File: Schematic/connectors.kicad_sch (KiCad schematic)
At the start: 42 parts, among them U14 HDGC1002WR-S-4P, U15 HDGC1002WR-S-4P, U16 HDGC1002WR-S-4P, U17 HDGC1002WR-S-4P, U18 HDGC1002WR-S-4P, U19 HDGC1002WR-S-4P, U20 HDGC1002WR-S-4P, U21 HDGC1002WR-S-8P, U22 HDGC1002WR-S-8P, U23 HDGC1002WR-S-6P, U24 HDGC1002WR-S-6P

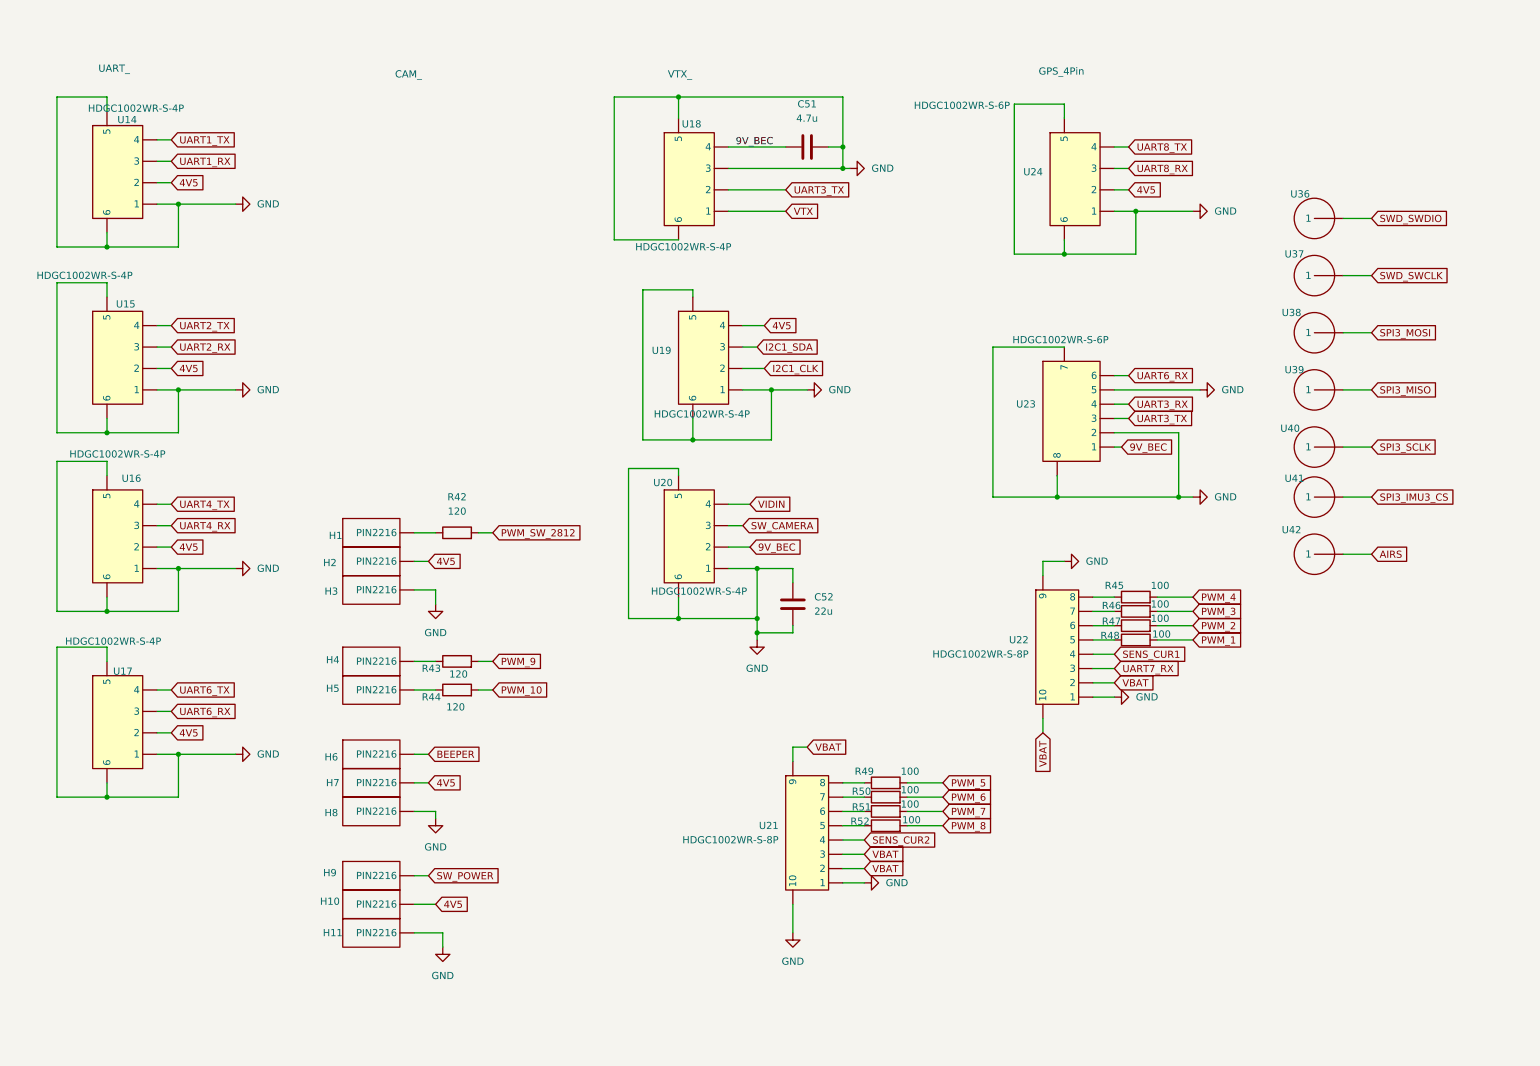
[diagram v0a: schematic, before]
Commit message: schematic fully finished, every footprint assigned, still electrical checking to do
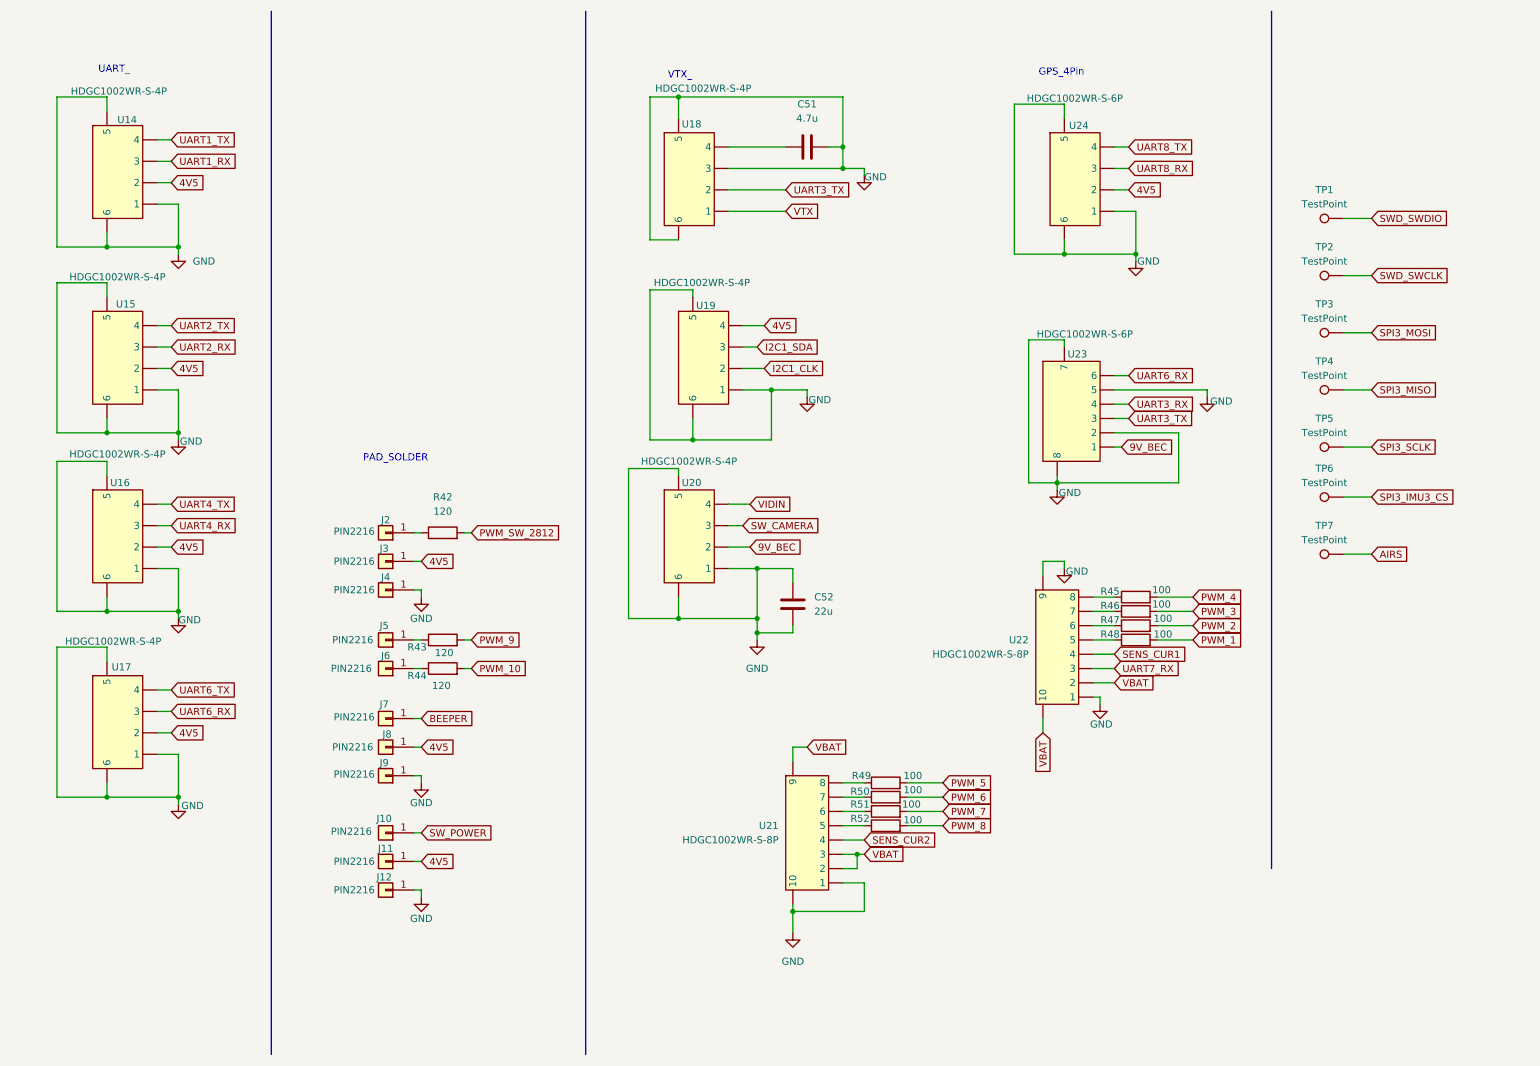
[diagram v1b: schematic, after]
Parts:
- removed H1, H10, H11, H2, H3, H4, H5, H6, H7, H8, H9: ~, symbol fclib:ws2812_
- removed U36, U37, U38, U39, U40, U41, U42: ~, symbol fclib:circular_pin
- added J10, J11, J12, J2, J3, J4, J5, J6, J7, J8, J9: PIN2216, fch7_fp:SolderPad_1x01_SMD_2.2x1.6mm, symbol Connector_Generic:Conn_01x01
- added TP1, TP2, TP3, TP4, TP5, TP6, TP7: TestPoint, TestPoint:TestPoint_Pad_1.0x1.0mm, symbol Connector:TestPoint
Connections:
- net 4V5: now also J11.1 (Pin_1), J3.1 (Pin_1), J8.1 (Pin_1)
- net 9V_BEC: no longer C51.1, U18. (1)
- net AIRS: now also TP7.1
- net BEEPER: now also J7.1 (Pin_1)
- net GND: now also J12.1 (Pin_1), J4.1 (Pin_1), J9.1 (Pin_1)
- net SPI3_IMU3_CS: now also TP6.1
- net SPI3_MISO: now also TP4.1
- net SPI3_MOSI: now also TP3.1
- net SPI3_SCLK: now also TP5.1
- net SWD_SWCLK: now also TP2.1
- net SWD_SWDIO: now also TP1.1
- net SW_POWER: now also J10.1 (Pin_1)
- net at R42.1: now also J2.1 (Pin_1)
- net at R43.1: now also J5.1 (Pin_1)
- net at R44.1: now also J6.1 (Pin_1)
- new net: C51.1, U18. (1)
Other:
- note added: "PAD_SOLDER"
- note removed: "CAM_"
- moved on the sheet: R42, R43, R44

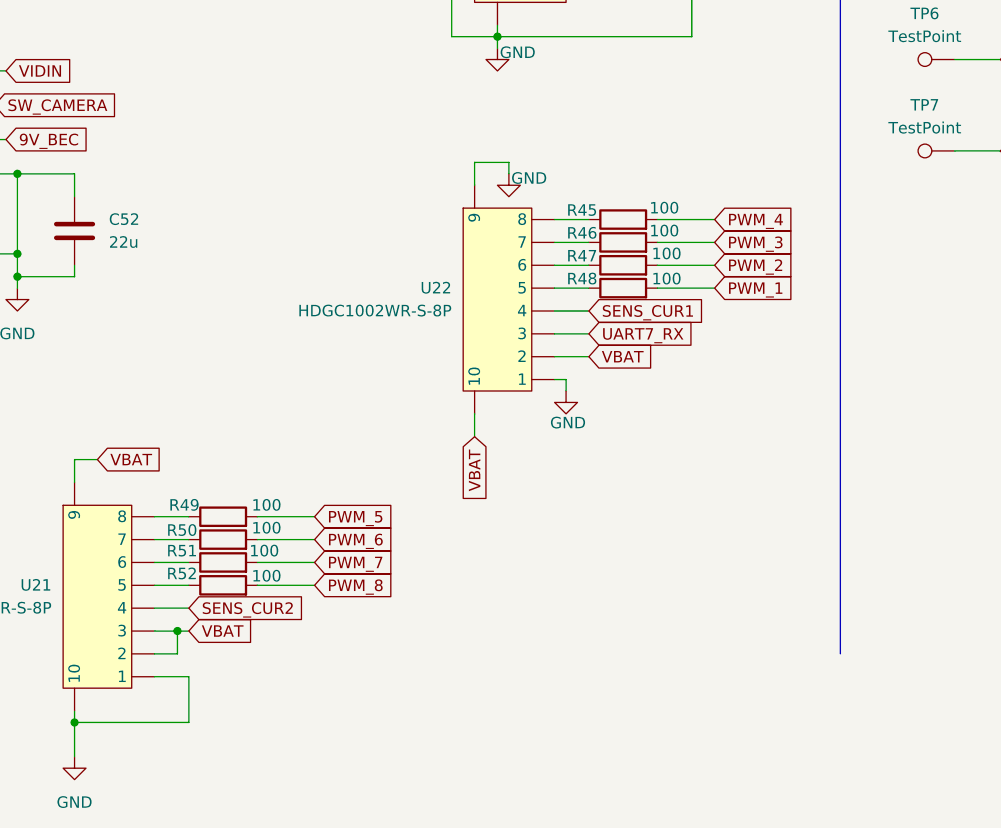
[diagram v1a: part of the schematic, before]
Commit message: reviewing and refactoring footprints and full schematic
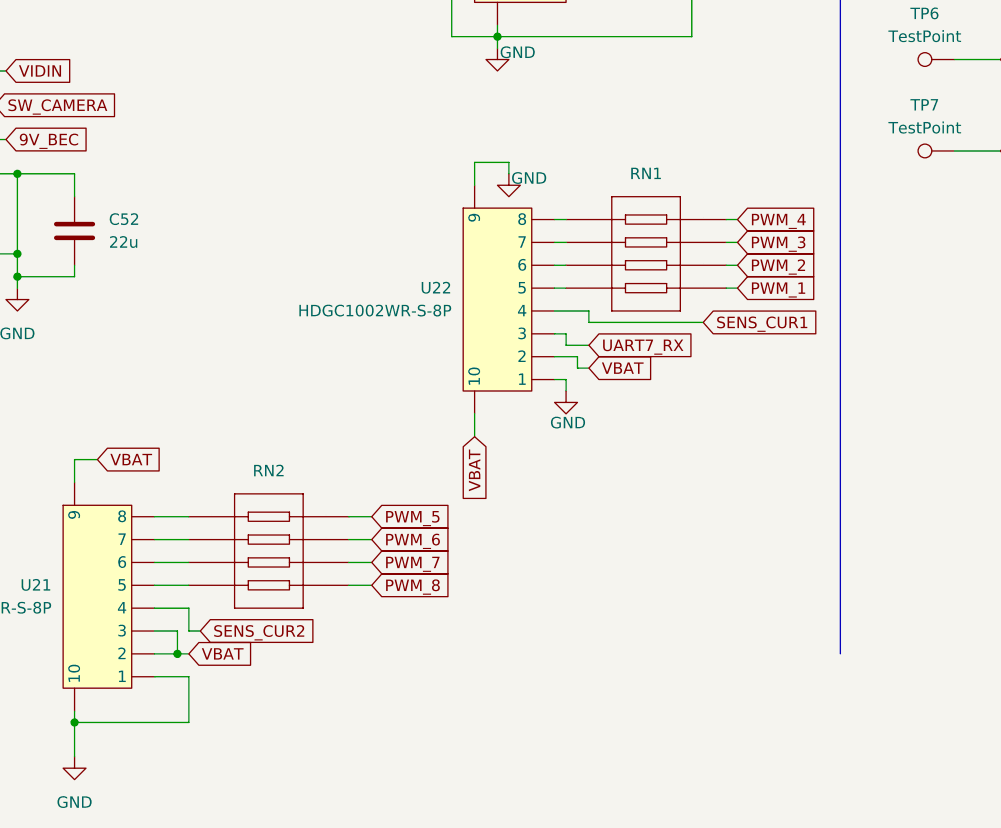
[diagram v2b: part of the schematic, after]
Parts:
- removed R45, R46, R47, R48, R49, R50, R51, R52: 100, Resistor_SMD:R_0603_1608Metric, symbol Device:R
- added RN1, RN2: 100Ω, ProLib_pcs_2025-11-25 (1):RES-ARRAY-SMD_0603-8P-L3.2-W1.6-BL, symbol fch7_sym:4D03WGJ0101T5E
- C51: footprint Capacitor_SMD:C_0805_2012Metric -> Capacitor_SMD:C_0603_1608Metric; MPN (none) -> CL10B105KO8NNNC; Manufacturer (none) -> SAMSUNG
- C52: footprint Capacitor_SMD:C_1210_3225Metric -> Capacitor_SMD:C_0805_2012Metric; MPN (none) -> CL21A226MAQNNNE; Manufacturer (none) -> SAMSUNG
- R42, R43, R44: MPN (none) -> 0603WAF1200T5E; Manufacturer (none) -> UNI-ROYAL
- U14, U15, U16, U17, U18, U19, U20: MPN (none) -> HDGC1002WR-S-4P; Manufacturer (none) -> HDGC
- U21, U22: MPN (none) -> HDGC1002WR-S-8P; Manufacturer (none) -> HDGC
- U23, U24: MPN (none) -> HDGC1002WR-S-6P; Manufacturer (none) -> HDGC
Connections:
- net PWM_1: now also RN1.5
- net PWM_2: now also RN1.6
- net PWM_3: now also RN1.7
- net PWM_4: now also RN1.8
- net PWM_5: now also RN2.8
- net PWM_6: now also RN2.7
- net PWM_7: now also RN2.6
- net PWM_8: now also RN2.5
- new net: RN1.1, U22. (1)
- new net: RN1.2, U22. (1)
- new net: RN1.3, U22. (1)
- new net: RN1.4, U22. (1)
- new net: RN2.1, U21. (1)
- new net: RN2.2, U21. (1)
- new net: RN2.3, U21. (1)
- new net: RN2.4, U21. (1)

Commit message: Update schematic and footprint libraries with various component modifications
- Updated fp-info-cache with new component details and footprint changes.
- Modified osd.kicad_sch to correct pin types and add no_connect entries.
- Adjusted rf_rx.kicad_sch to fix pin assignments and update component properties.
- Enhanced sensors.kicad_sch with new properties for QMC5883L and SPL06-001 sensors.
- Added new libraries to sym-lib-table and fp-lib-table for better organization and access to components.
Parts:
- RN1, RN2: MPN 4D03WGJ0101T5E -> (none)

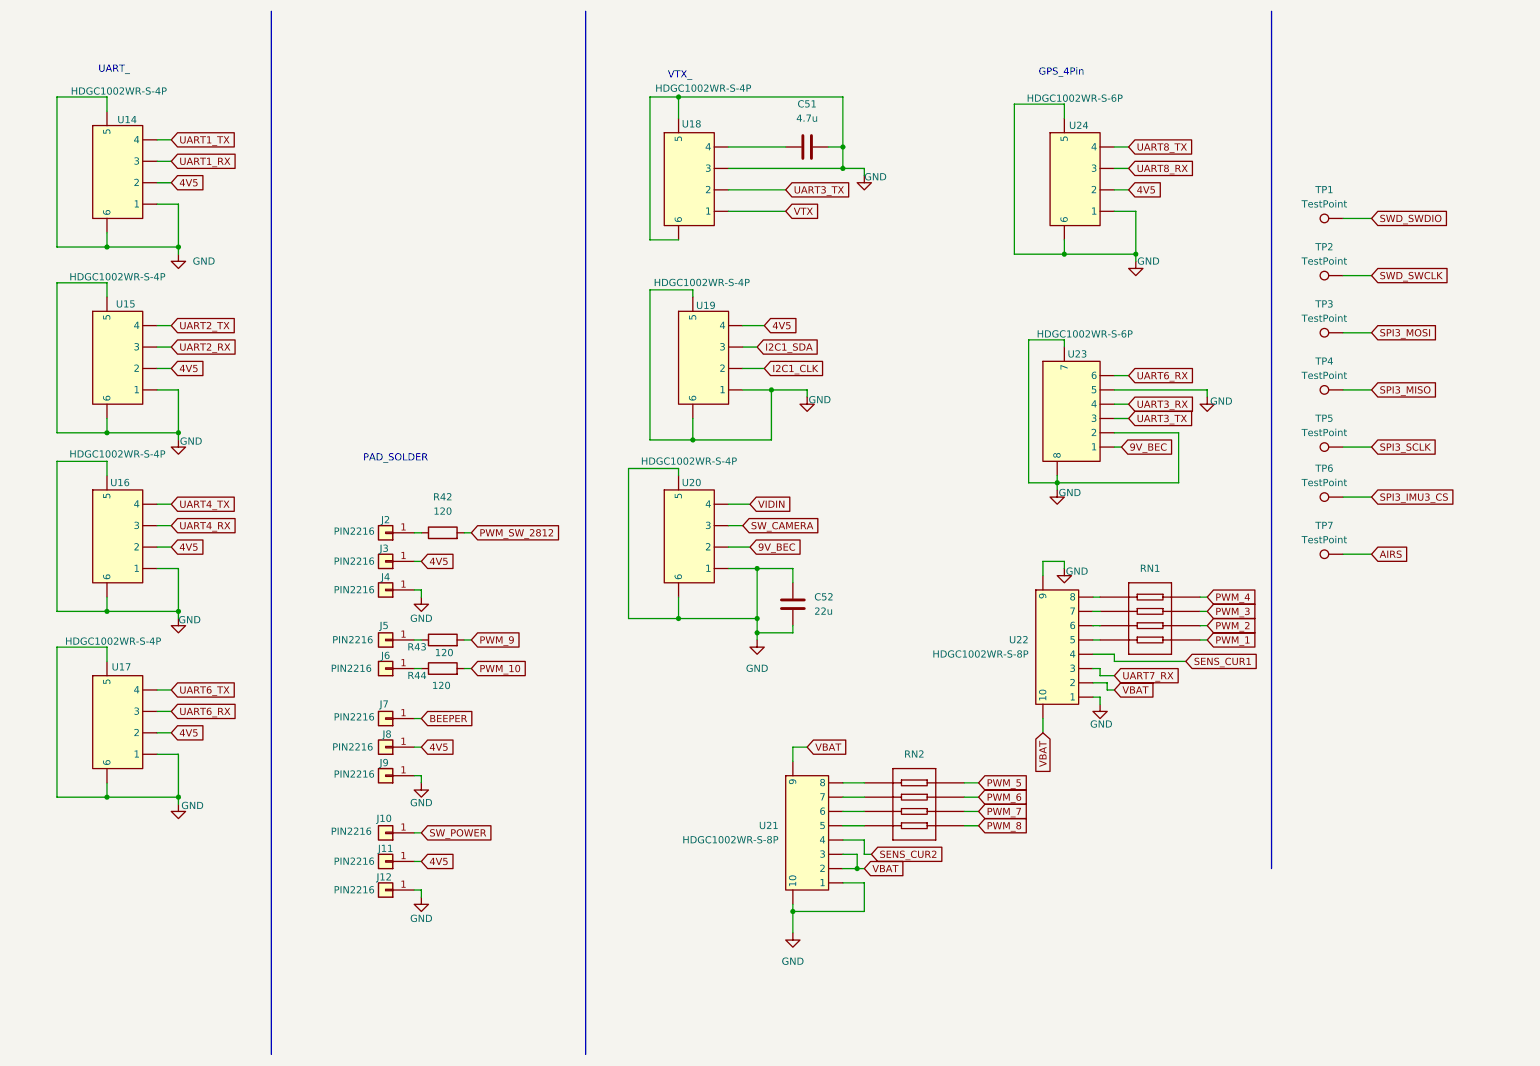
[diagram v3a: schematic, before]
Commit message: Refactor fp-lib-table: Remove unused libraries and update description for fch7_fp
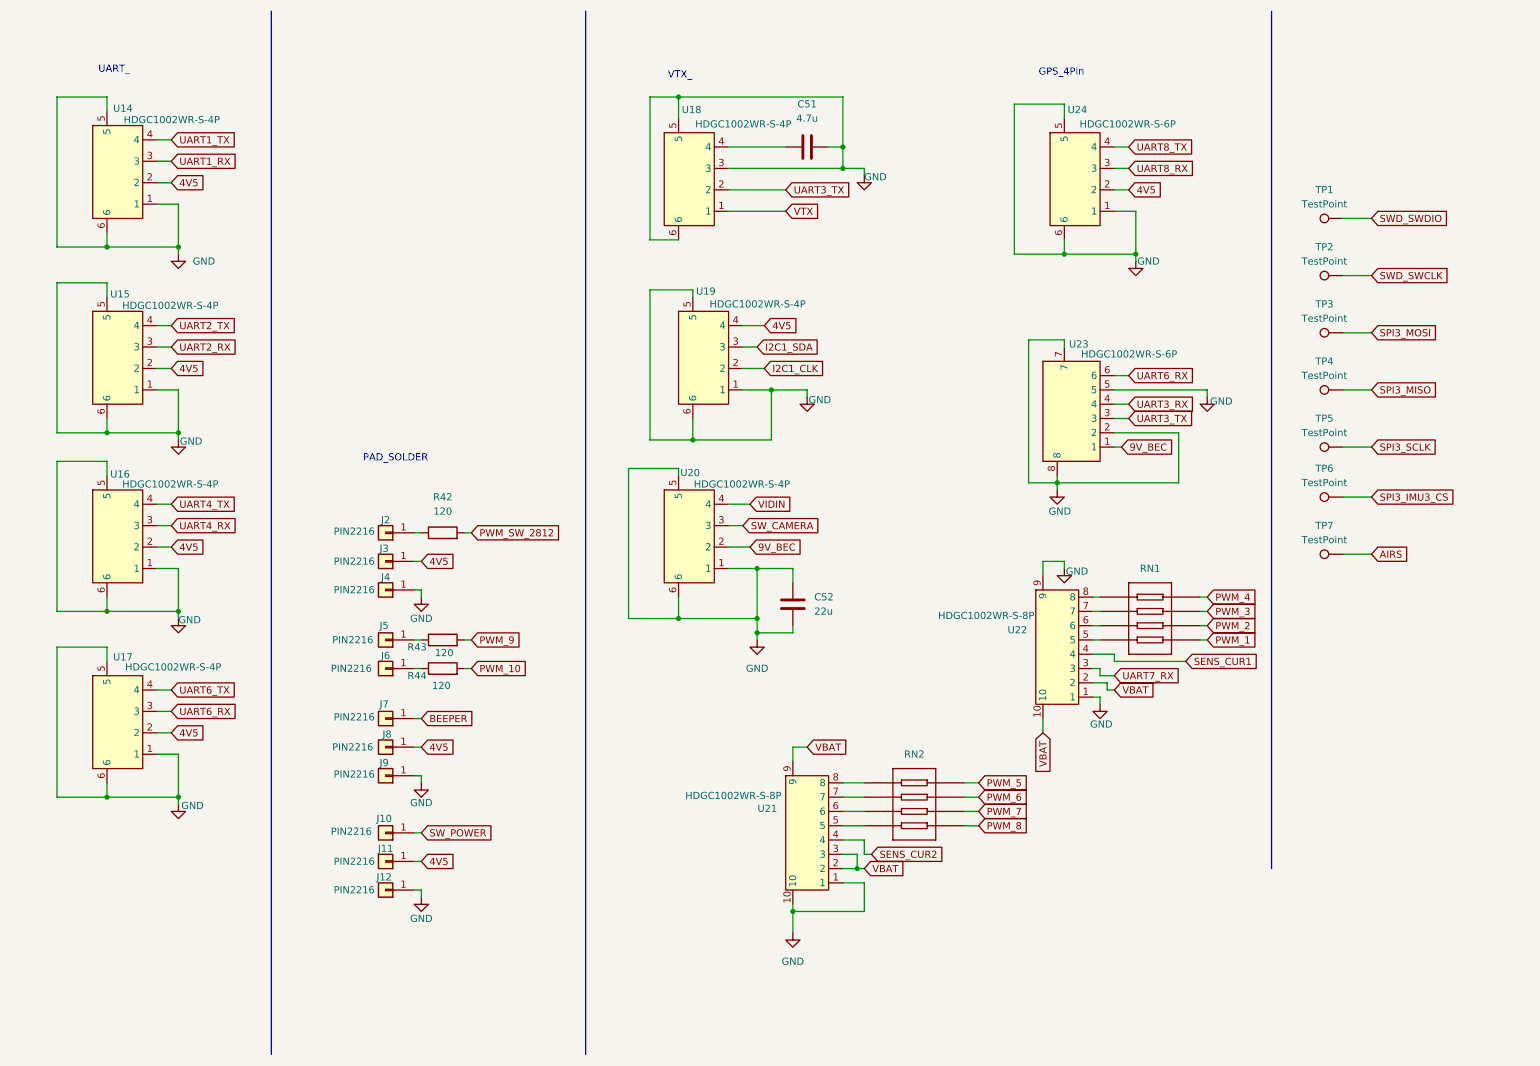
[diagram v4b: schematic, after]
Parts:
- RN1, RN2: footprint ProLib_pcs_2025-11-25 (1):RES-ARRAY-SMD_0603-8P-L3.2-W1.6-BL -> fch7_fp:RES-ARRAY-SMD_0603-8P-L3.2-W1.6-BL
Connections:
- net 4V5: now also U14.2, U15.2, U16.2, U17.2, U19.4, U24.2; no longer U14. (1), U15. (1), U16. (1), U17. (1), U19. (1), U24. (1)
- net 9V_BEC: now also U20.2, U23.1; no longer U20. (1), U23. (1)
- net GND: now also U14.1, U14.5, U14.6, U15.1, U15.5, U15.6, U16.1, U16.5, U16.6, U17.1, U17.5, U17.6, U18.3, U18.5, U18.6, U19.1, U19.5, U19.6, U20.1, U20.5, U20.6, U21.1, U21.10, U22.1, U22.9, U23.2, U23.5, U23.7, U23.8, U24.1, U24.5, U24.6; no longer U14. (1), U15. (1), U16. (1), U17. (1), U18. (1), U19. (1), U20. (1), U21. (1), U22. (1), U24. (1)
- net I2C1_CLK: now also U19.2; no longer U19. (1)
- net I2C1_SDA: now also U19.3; no longer U19. (1)
- net SENS_CUR1: now also U22.4; no longer U22. (1)
- net SENS_CUR2: now also U21.4; no longer U21. (1)
- net SW_CAMERA: now also U20.3; no longer U20. (1)
- net UART1_RX: now also U14.3; no longer U14. (1)
- net UART1_TX: now also U14.4; no longer U14. (1)
- net UART2_RX: now also U15.3; no longer U15. (1)
- net UART2_TX: now also U15.4; no longer U15. (1)
- net UART3_RX: now also U23.4; no longer U23. (1)
- net UART3_TX: now also U18.2, U23.3; no longer U18. (1), U23. (1)
- net UART4_RX: now also U16.3; no longer U16. (1)
- net UART4_TX: now also U16.4; no longer U16. (1)
- net UART6_RX: now also U17.3, U23.6; no longer U17. (1), U23. (1)
- net UART6_TX: now also U17.4; no longer U17. (1)
- net UART7_RX: now also U22.3; no longer U22. (1)
- net UART8_RX: now also U24.3; no longer U24. (1)
- net UART8_TX: now also U24.4; no longer U24. (1)
- net VBAT: now also U21.2, U21.3, U21.9, U22.10, U22.2; no longer U21. (1), U22. (1)
- net VIDIN: now also U20.4; no longer U20. (1)
- net VTX: now also U18.1; no longer U18. (1)
- net at RN2.1: now also U21.8; no longer U21. (1)
- net at RN2.2: now also U21.7; no longer U21. (1)
- net at RN2.3: now also U21.6; no longer U21. (1)
- net at RN2.4: now also U21.5; no longer U21. (1)
- net at C51.1: now also U18.4; no longer U18. (1)
- net at RN1.1: now also U22.8; no longer U22. (1)
- net at RN1.2: now also U22.7; no longer U22. (1)
- net at RN1.3: now also U22.6; no longer U22. (1)
- net at RN1.4: now also U22.5; no longer U22. (1)
